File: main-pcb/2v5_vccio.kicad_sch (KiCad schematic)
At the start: 1 part, among them U1 XC7S100-1FGGA484C

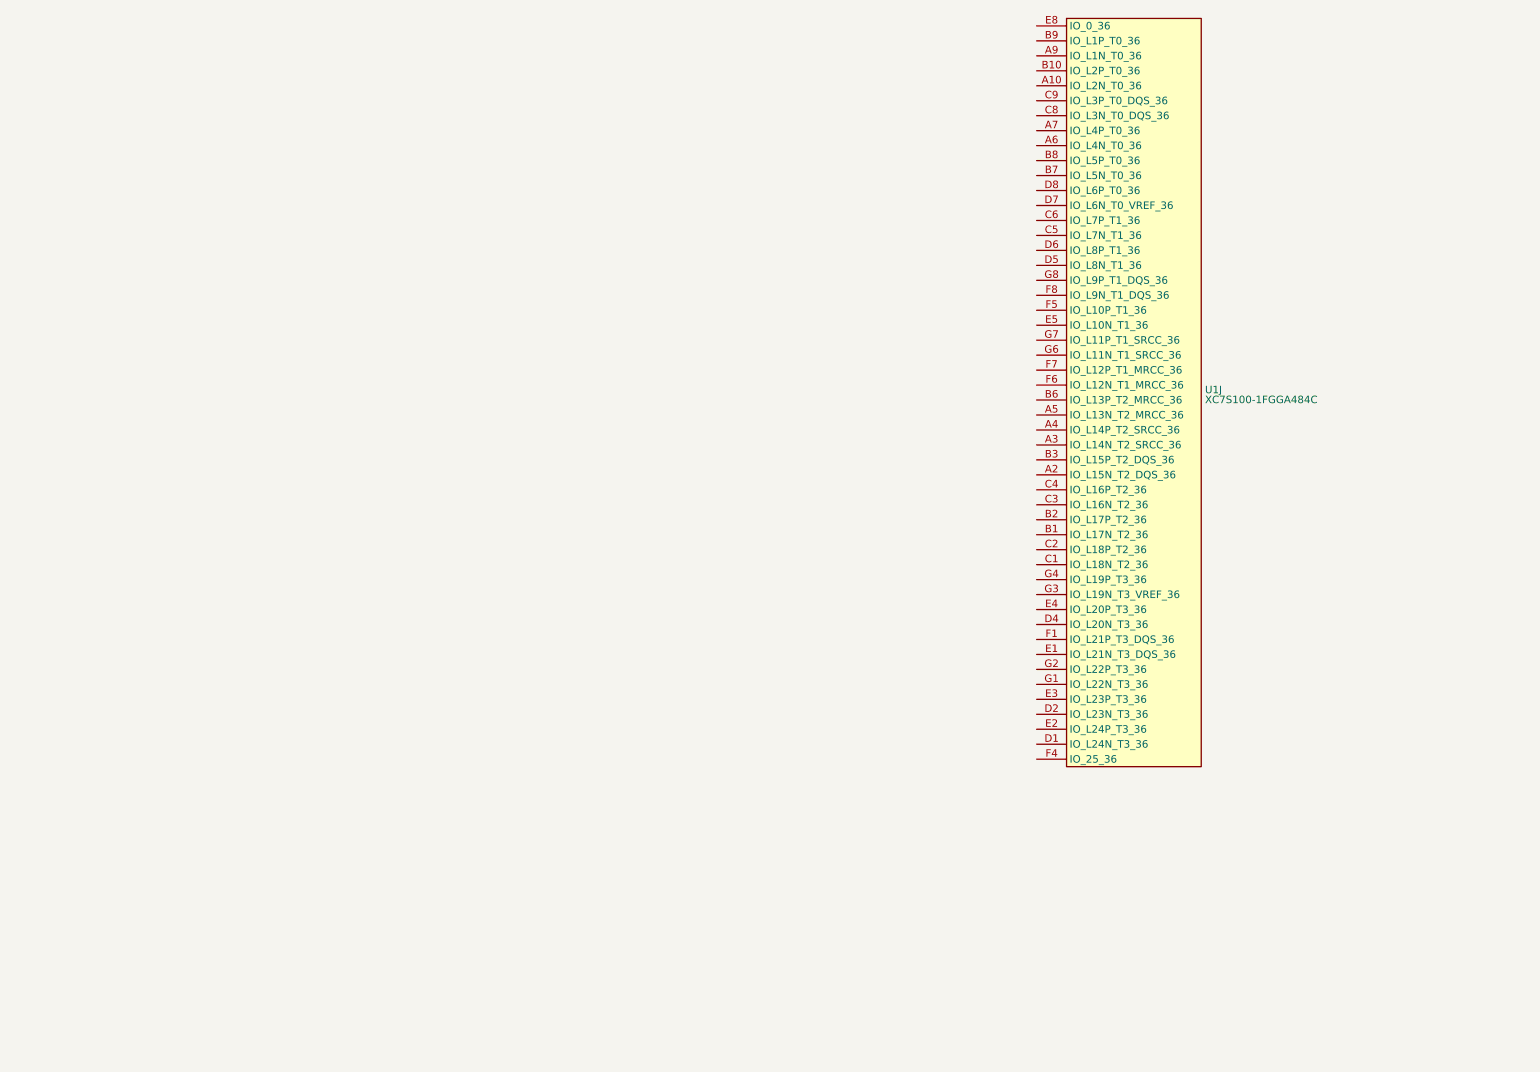
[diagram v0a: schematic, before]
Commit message: Initial design mostly done aside from USB connector, review, test points
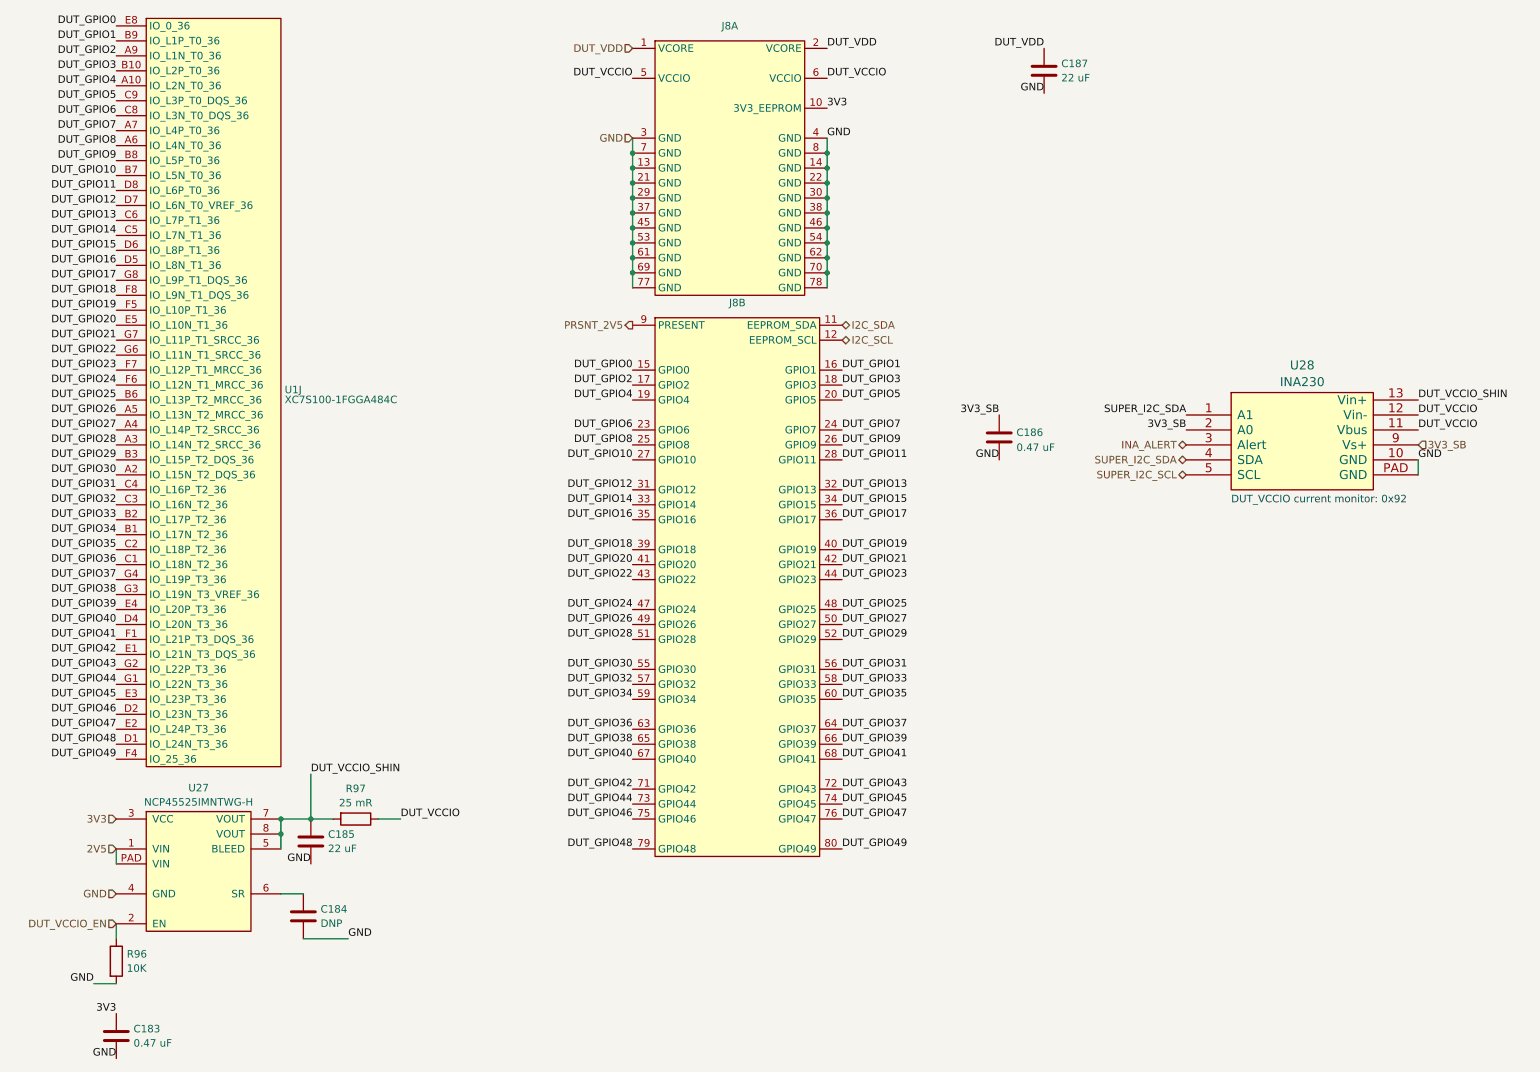
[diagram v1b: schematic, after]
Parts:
- added C183: 0.47 uF, symbol device:C
- added C184: DNP, symbol device:C
- added C185, C187: 22 uF, symbol device:C
- added C186: 0.47 uF, azonenberg_pcb:EIA_0402_CAP_NOSILK, symbol device:C
- added J8: ~, symbol special-azonenberg:CONN_DUMPTRUCK_HOST
- added R96: 10K, symbol device:R
- added R97: 25 mR, symbol passive-azonenberg:R_PWR
- added U27: NCP45525IMNTWG-H, symbol power-azonenberg:NCP45525
- added U28: INA230, azonenberg_pcb:QFN_16_0.5MM_3x3MM, symbol special-azonenberg:INA230
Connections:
- net DUT_GPIO4: now reaches U1.A10 (IO_L2N_T0_36)
- net DUT_GPIO4: now also J8.19 (GPIO4)
- net DUT_GPIO30: now reaches U1.A2 (IO_L15N_T2_DQS_36)
- net DUT_GPIO30: now also J8.55 (GPIO30)
- net DUT_GPIO28: now reaches U1.A3 (IO_L14N_T2_SRCC_36)
- net DUT_GPIO28: now also J8.51 (GPIO28)
- net DUT_GPIO27: now reaches U1.A4 (IO_L14P_T2_SRCC_36)
- net DUT_GPIO27: now also J8.50 (GPIO27)
- net DUT_GPIO26: now reaches U1.A5 (IO_L13N_T2_MRCC_36)
- net DUT_GPIO26: now also J8.49 (GPIO26)
- net DUT_GPIO8: now reaches U1.A6 (IO_L4N_T0_36)
- net DUT_GPIO8: now also J8.25 (GPIO8)
- net DUT_GPIO7: now reaches U1.A7 (IO_L4P_T0_36)
- net DUT_GPIO7: now also J8.24 (GPIO7)
- net DUT_GPIO2: now reaches U1.A9 (IO_L1N_T0_36)
- net DUT_GPIO2: now also J8.17 (GPIO2)
- net DUT_GPIO34: now reaches U1.B1 (IO_L17N_T2_36)
- net DUT_GPIO34: now also J8.59 (GPIO34)
- net DUT_GPIO3: now reaches U1.B10 (IO_L2P_T0_36)
- net DUT_GPIO3: now also J8.18 (GPIO3)
- net DUT_GPIO33: now reaches U1.B2 (IO_L17P_T2_36)
- net DUT_GPIO33: now also J8.58 (GPIO33)
- net DUT_GPIO29: now reaches U1.B3 (IO_L15P_T2_DQS_36)
- net DUT_GPIO29: now also J8.52 (GPIO29)
- net DUT_GPIO25: now reaches U1.B6 (IO_L13P_T2_MRCC_36)
- net DUT_GPIO25: now also J8.48 (GPIO25)
- net DUT_GPIO10: now reaches U1.B7 (IO_L5N_T0_36)
- net DUT_GPIO10: now also J8.27 (GPIO10)
- net DUT_GPIO9: now reaches U1.B8 (IO_L5P_T0_36)
- net DUT_GPIO9: now also J8.26 (GPIO9)
- net DUT_GPIO1: now reaches U1.B9 (IO_L1P_T0_36)
- net DUT_GPIO1: now also J8.16 (GPIO1)
- net DUT_GPIO36: now reaches U1.C1 (IO_L18N_T2_36)
- net DUT_GPIO36: now also J8.63 (GPIO36)
- net DUT_GPIO35: now reaches U1.C2 (IO_L18P_T2_36)
- net DUT_GPIO35: now also J8.60 (GPIO35)
- net DUT_GPIO32: now reaches U1.C3 (IO_L16N_T2_36)
- net DUT_GPIO32: now also J8.57 (GPIO32)
- net DUT_GPIO31: now reaches U1.C4 (IO_L16P_T2_36)
- net DUT_GPIO31: now also J8.56 (GPIO31)
- net DUT_GPIO14: now reaches U1.C5 (IO_L7N_T1_36)
- net DUT_GPIO14: now also J8.33 (GPIO14)
- net DUT_GPIO13: now reaches U1.C6 (IO_L7P_T1_36)
- net DUT_GPIO13: now also J8.32 (GPIO13)
- net DUT_GPIO6: now reaches U1.C8 (IO_L3N_T0_DQS_36)
- net DUT_GPIO6: now also J8.23 (GPIO6)
- net DUT_GPIO5: now reaches U1.C9 (IO_L3P_T0_DQS_36)
- net DUT_GPIO5: now also J8.20 (GPIO5)
- net DUT_GPIO48: now reaches U1.D1 (IO_L24N_T3_36)
- net DUT_GPIO48: now also J8.79 (GPIO48)
- net DUT_GPIO46: now reaches U1.D2 (IO_L23N_T3_36)
- net DUT_GPIO46: now also J8.75 (GPIO46)
- net DUT_GPIO40: now reaches U1.D4 (IO_L20N_T3_36)
- net DUT_GPIO40: now also J8.67 (GPIO40)
- net DUT_GPIO16: now reaches U1.D5 (IO_L8N_T1_36)
- net DUT_GPIO16: now also J8.35 (GPIO16)
- net DUT_GPIO15: now reaches U1.D6 (IO_L8P_T1_36)
- net DUT_GPIO15: now also J8.34 (GPIO15)
- net DUT_GPIO12: now reaches U1.D7 (IO_L6N_T0_VREF_36)
- net DUT_GPIO12: now also J8.31 (GPIO12)
- net DUT_GPIO11: now reaches U1.D8 (IO_L6P_T0_36)
- net DUT_GPIO11: now also J8.28 (GPIO11)
- net DUT_GPIO42: now reaches U1.E1 (IO_L21N_T3_DQS_36)
- net DUT_GPIO42: now also J8.71 (GPIO42)
- net DUT_GPIO47: now reaches U1.E2 (IO_L24P_T3_36)
- net DUT_GPIO47: now also J8.76 (GPIO47)
- net DUT_GPIO45: now reaches U1.E3 (IO_L23P_T3_36)
- net DUT_GPIO45: now also J8.74 (GPIO45)
- net DUT_GPIO39: now reaches U1.E4 (IO_L20P_T3_36)
- net DUT_GPIO39: now also J8.66 (GPIO39)
- net DUT_GPIO20: now reaches U1.E5 (IO_L10N_T1_36)
- net DUT_GPIO20: now also J8.41 (GPIO20)
- net DUT_GPIO0: now reaches U1.E8 (IO_0_36)
- net DUT_GPIO0: now also J8.15 (GPIO0)
- net DUT_GPIO41: now reaches U1.F1 (IO_L21P_T3_DQS_36)
- net DUT_GPIO41: now also J8.68 (GPIO41)
- net DUT_GPIO49: now reaches U1.F4 (IO_25_36)
- net DUT_GPIO49: now also J8.80 (GPIO49)
- net DUT_GPIO19: now reaches U1.F5 (IO_L10P_T1_36)
- net DUT_GPIO19: now also J8.40 (GPIO19)
- net DUT_GPIO24: now reaches U1.F6 (IO_L12N_T1_MRCC_36)
- net DUT_GPIO24: now also J8.47 (GPIO24)
- net DUT_GPIO23: now reaches U1.F7 (IO_L12P_T1_MRCC_36)
- net DUT_GPIO23: now also J8.44 (GPIO23)
- net DUT_GPIO18: now reaches U1.F8 (IO_L9N_T1_DQS_36)
- net DUT_GPIO18: now also J8.39 (GPIO18)
- net DUT_GPIO44: now reaches U1.G1 (IO_L22N_T3_36)
- net DUT_GPIO44: now also J8.73 (GPIO44)
- net DUT_GPIO43: now reaches U1.G2 (IO_L22P_T3_36)
- net DUT_GPIO43: now also J8.72 (GPIO43)
- net DUT_GPIO38: now reaches U1.G3 (IO_L19N_T3_VREF_36)
- net DUT_GPIO38: now also J8.65 (GPIO38)
- net DUT_GPIO37: now reaches U1.G4 (IO_L19P_T3_36)
- net DUT_GPIO37: now also J8.64 (GPIO37)
- net DUT_GPIO22: now reaches U1.G6 (IO_L11N_T1_SRCC_36)
- net DUT_GPIO22: now also J8.43 (GPIO22)
- net DUT_GPIO21: now reaches U1.G7 (IO_L11P_T1_SRCC_36)
- net DUT_GPIO21: now also J8.42 (GPIO21)
- net DUT_GPIO17: now reaches U1.G8 (IO_L9P_T1_DQS_36)
- net DUT_GPIO17: now also J8.36 (GPIO17)
- new net: C184.1, U27.6 (SR)
- new net 2V5: U27.1 (VIN), U27.PAD (VIN)
- new net 3V3: C183.1, J8.10 (3V3_EEPROM), U27.3 (VCC)
- new net 3V3_SB: C186.1, U28.2 (A0), U28.9 (Vs+)
- new net DUT_VCCIO: J8.5 (VCCIO), J8.6 (VCCIO), R97.1, U28.11 (Vbus), U28.12 (Vin-)
- new net DUT_VCCIO_EN: R96.1, U27.2 (EN)
- new net DUT_VCCIO_SHIN: C185.1, R97.2, U27.5 (BLEED), U27.7 (VOUT), U27.8 (VOUT), U28.13 (Vin+)
- new net DUT_VDD: C187.1, J8.1 (VCORE), J8.2 (VCORE)
- new net GND: C183.2, C184.2, C185.2, C186.2, C187.2, J8.13 (GND), J8.14 (GND), J8.21 (GND), J8.22 (GND), J8.29 (GND), J8.3 (GND), J8.30 (GND), J8.37 (GND), J8.38 (GND), J8.4 (GND), J8.45 (GND), J8.46 (GND), J8.53 (GND), J8.54 (GND), J8.61 (GND), J8.62 (GND), J8.69 (GND), J8.7 (GND), J8.70 (GND), J8.77 (GND), J8.78 (GND), J8.8 (GND), R96.2, U27.4 (GND), U28.10 (GND), U28.PAD (GND)
- new net I2C_SCL: J8.12 (EEPROM_SCL)
- new net I2C_SDA: J8.11 (EEPROM_SDA)
- new net INA_ALERT: U28.3 (Alert)
- new net PRSNT_2V5: J8.9 (PRESENT)
- new net SUPER_I2C_SCL: U28.5 (SCL)
- new net SUPER_I2C_SDA: U28.1 (A1), U28.4 (SDA)
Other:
- note added: "DUT_VCCIO current monitor: 0x92"
- moved on the sheet: U1J

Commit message: More schematic tweaks and test points
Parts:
- C183, C184: footprint (none) -> azonenberg_pcb:EIA_0402_CAP_NOSILK
- J8: value ~ -> CONN_DUMPTRUCK_HOST
- R96, R97: footprint (none) -> azonenberg_pcb:EIA_0402_RES_NOSILK
- U27: footprint (none) -> azonenberg_pcb:DFN_8_0.5MM_2x2MM
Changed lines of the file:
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@@
 			)
 		)
-		(property "Footprint" ""
+		(property "Footprint" "azonenberg_pcb:DFN_8_0.5MM_2x2MM"
 			(at 52.07 172.72 0)
 			(effects
@@
 			)
 		)
-		(property "Footprint" ""
+		(property "Footprint" "azonenberg_pcb:EIA_0402_RES_NOSILK"
 			(at 87.63 151.892 90)
 			(effects
@@
 			)
 		)
-		(property "Footprint" ""
+		(property "Footprint" "azonenberg_pcb:EIA_0402_RES_NOSILK"
 			(at 45.212 177.8 90)
 			(effects
@@
 			)
 		)
-		(property "Footprint" ""
+		(property "Footprint" "azonenberg_pcb:EIA_0402_CAP_NOSILK"
 			(at 79.7052 173.99 0)
 			(effects
@@
 			)
 		)
-		(property "Footprint" ""
+		(property "Footprint" "azonenberg_pcb:EIA_0402_CAP_NOSILK"
 			(at 47.9552 194.31 0)
 			(effects
@@
 			)
 		)
-		(property "Value" "~"
+		(property "Value" "CONN_DUMPTRUCK_HOST"
 			(at 152.4 67.7299 0)
 			(effects
@@
 			)
 		)
-		(property "Value" "~"
+		(property "Value" "CONN_DUMPTRUCK_HOST"
 			(at 151.13 20.7399 0)
 			(effects

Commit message: Added some RGB LEDs, changed a few voltage dividers to match what was in stock. Time for next round of review.
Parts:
- C185, C187: footprint (none) -> azonenberg_pcb:EIA_1206_CAP_NOSILK
- J8: footprint (none) -> azonenberg_pcb:CONN_SAMTEC_BTE-040-01-F-D-A-K
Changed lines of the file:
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@@
 	(title_block
 		(title "DUMPTRUCK flash dumper")
-		(date "2024-10-16")
+		(date "2024-10-17")
 		(rev "0.1")
 		(company "Antikernel Labs")
@@
 			)
 		)
-		(property "Footprint" ""
+		(property "Footprint" "azonenberg_pcb:EIA_1206_CAP_NOSILK"
 			(at 80.9752 161.29 0)
 			(effects
@@
 			)
 		)
-		(property "Footprint" ""
+		(property "Footprint" "azonenberg_pcb:CONN_SAMTEC_BTE-040-01-F-D-A-K"
 			(at 138.43 160.02 0)
 			(effects
@@
 			)
 		)
-		(property "Footprint" ""
+		(property "Footprint" "azonenberg_pcb:EIA_1206_CAP_NOSILK"
 			(at 205.4352 30.48 0)
 			(effects
@@
 			)
 		)
-		(property "Footprint" ""
+		(property "Footprint" "azonenberg_pcb:CONN_SAMTEC_BTE-040-01-F-D-A-K"
 			(at 138.43 64.77 0)
 			(effects

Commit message: Finished schematic review
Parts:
- R96: value 10K -> DNP
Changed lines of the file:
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@@
 			)
 		)
-		(property "Value" "10K"
+		(property "Value" "DNP"
 			(at 48.768 179.0121 0)
 			(effects
